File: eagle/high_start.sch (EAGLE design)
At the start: 34 parts, among them IC1 7805TV, Q1 16Mhz, Q2 IRF510, Q3 IRF510, Q4 IRF510, U2 ATMEGA328P_PDIP

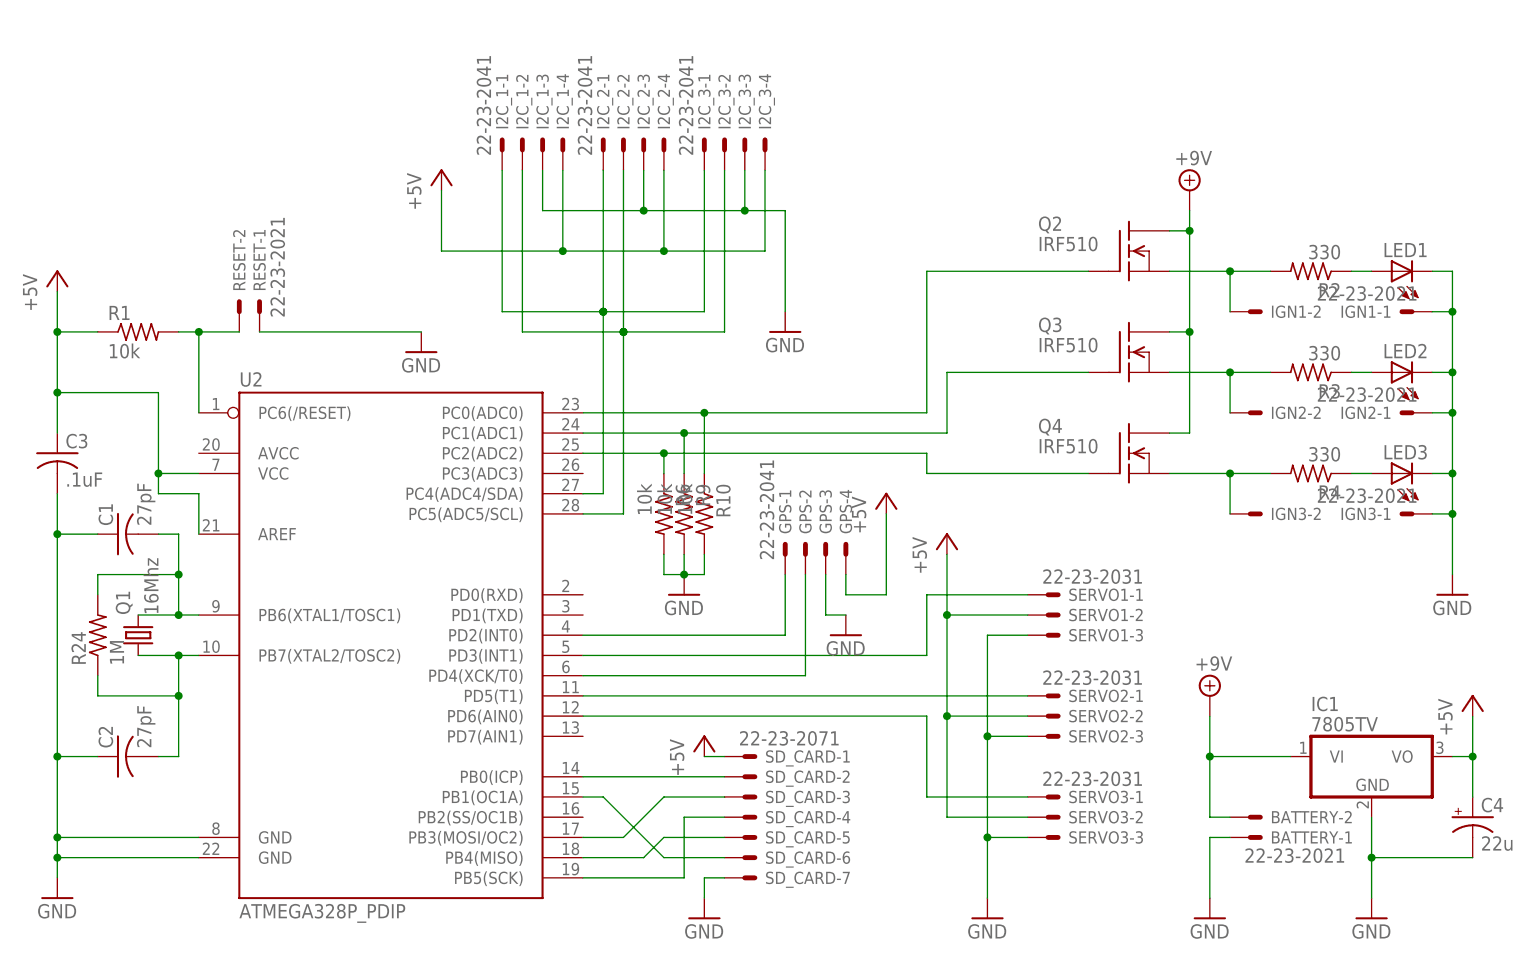
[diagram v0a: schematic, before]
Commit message: moved igniter FETs to low side
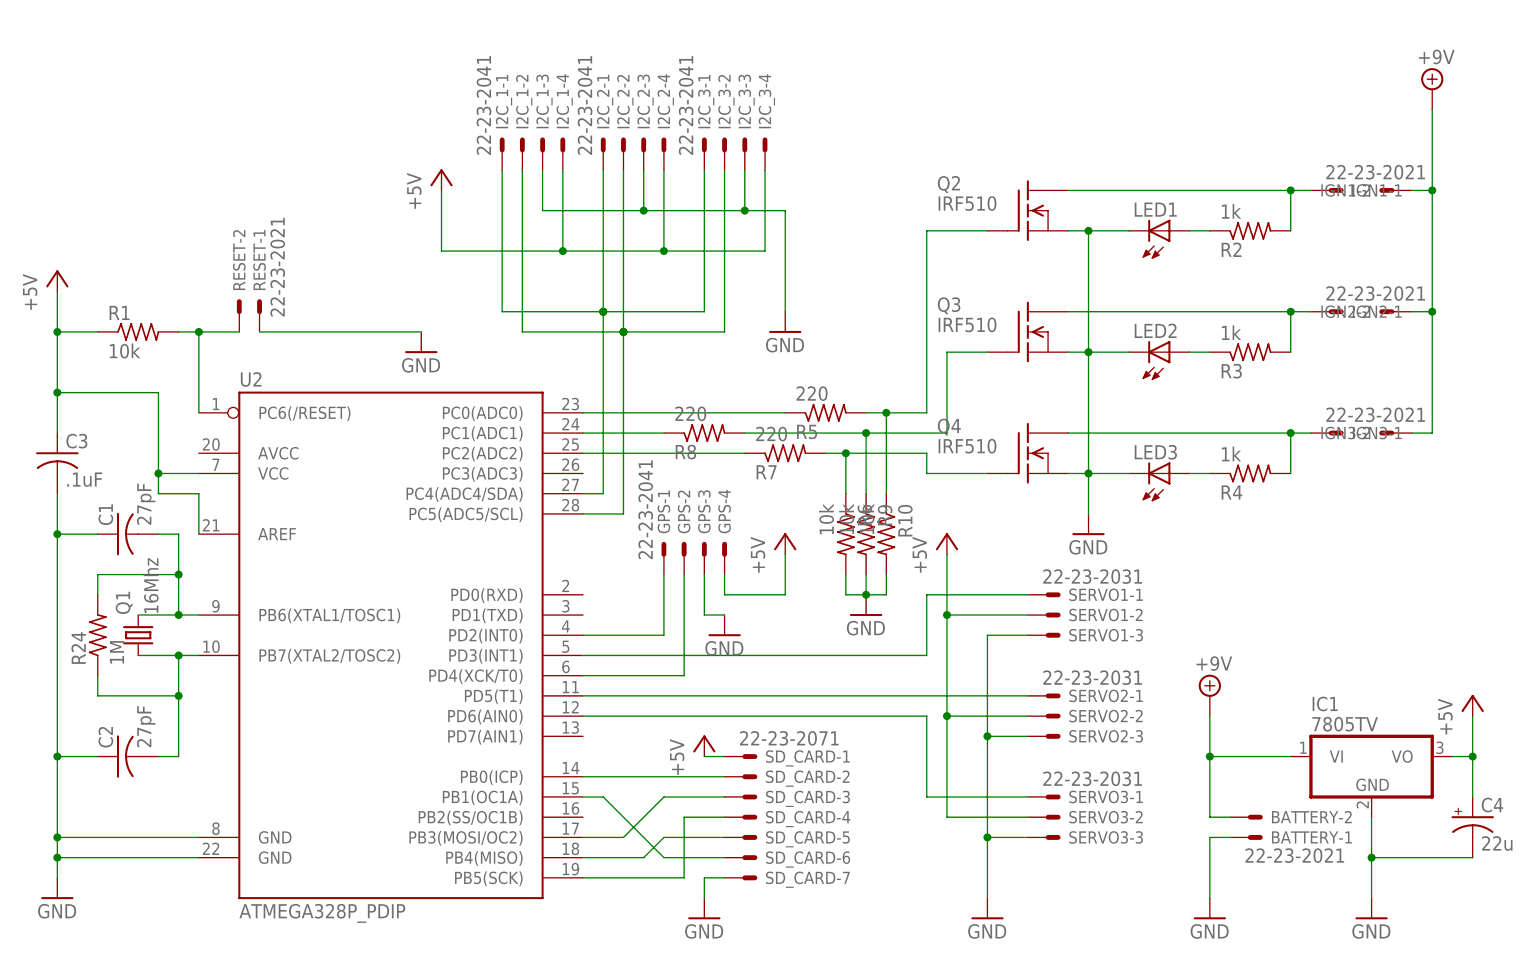
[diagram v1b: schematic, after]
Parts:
- added R5, R7, R8: 220, rcl:R-US_0207/7
- R2, R3, R4: value 330 -> 1k
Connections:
- new net N$12: IGN1-1.S, Q2.D, R2.2
- new net N$13: IGN2-1.S, Q3.D, R3.2
- new net N$14: IGN3-1.S, Q4.D, R4.2
- net +9V: now also IGN1-2.S, IGN2-2.S, IGN3-2.S; no longer Q2.D, Q3.D, Q4.D
- net GND: now also Q2.S, Q3.S, Q4.S; no longer IGN1-1.S, IGN2-1.S, IGN3-1.S
- net N$18: now also R5.2; no longer U2.PC0(ADC0)
- net N$19: now also R8.2; no longer U2.PC1(ADC1)
- net N$20: now also R7.2; no longer U2.PC2(ADC2)
- net N$24: now also R5.1, U2.PC0(ADC0); no longer IGN1-2.S, Q2.S, R2.2
- net N$25: now also R7.1, U2.PC2(ADC2); no longer IGN2-2.S, Q3.S, R3.2
- net N$26: now also R8.1, U2.PC1(ADC1); no longer IGN3-2.S, Q4.S, R4.2
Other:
- moved on the sheet: GPS-1, GPS-2, GPS-3, GPS-4, IGN1-1, IGN1-2, IGN2-1, IGN2-2, IGN3-1, IGN3-2, LED1, LED2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

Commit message: janky rerouted
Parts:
- R10, R6, R9: device rcl:R-US_0207/2V -> rcl:R-US_0207/7
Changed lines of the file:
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@@
 <grid distance="0.1" unitdist="inch" unit="inch" style="lines" multiple="1" display="no" altdistance="0.01" altunitdist="inch" altunit="inch"/>
 <layers>
-<layer number="1" name="Top" color="4" fill="1" visible="no" active="no"/>
-<layer number="16" name="Bottom" color="1" fill="1" visible="no" active="no"/>
-<layer number="17" name="Pads" color="2" fill="1" visible="no" active="no"/>
-<layer number="18" name="Vias" color="2" fill="1" visible="no" active="no"/>
-<layer number="19" name="Unrouted" color="6" fill="1" visible="no" active="no"/>
-<layer number="20" name="Dimension" color="15" fill="1" visible="no" active="no"/>
-<layer number="21" name="tPlace" color="7" fill="1" visible="no" active="no"/>
-<layer number="22" name="bPlace" color="7" fill="1" visible="no" active="no"/>
-<layer number="23" name="tOrigins" color="15" fill="1" visible="no" active="no"/>
-<layer number="24" name="bOrigins" color="15" fill="1" visible="no" active="no"/>
-<layer number="25" name="tNames" color="7" fill="1" visible="no" active="no"/>
-<layer number="26" name="bNames" color="7" fill="1" visible="no" active="no"/>
-<layer number="27" name="tValues" color="7" fill="1" visible="no" active="no"/>
-<layer number="28" name="bValues" color="7" fill="1" visible="no" active="no"/>
+<layer number="1" name="Top" color="4" fill="1" visible="yes" active="no"/>
+<layer number="16" name="Bottom" color="1" fill="1" visible="yes" active="no"/>
+<layer number="17" name="Pads" color="2" fill="1" visible="yes" active="no"/>
+<layer number="18" name="Vias" color="2" fill="1" visible="yes" active="no"/>
+<layer number="19" name="Unrouted" color="6" fill="1" visible="yes" active="no"/>
+<layer number="20" name="Dimension" color="15" fill="1" visible="yes" active="no"/>
+<layer number="21" name="tPlace" color="7" fill="1" visible="yes" active="no"/>
+<layer number="22" name="bPlace" color="7" fill="1" visible="yes" active="no"/>
+<layer number="23" name="tOrigins" color="15" fill="1" visible="yes" active="no"/>
+<layer number="24" name="bOrigins" color="15" fill="1" visible="yes" active="no"/>
+<layer number="25" name="tNames" color="7" fill="1" visible="yes" active="no"/>
+<layer number="26" name="bNames" color="7" fill="1" visible="yes" active="no"/>
+<layer number="27" name="tValues" color="7" fill="1" visible="yes" active="no"/>
+<layer number="28" name="bValues" color="7" fill="1" visible="yes" active="no"/>
 <layer number="29" name="tStop" color="7" fill="3" visible="no" active="no"/>
 <layer number="30" name="bStop" color="7" fill="6" visible="no" active="no"/>
@@
 <layer number="35" name="tGlue" color="7" fill="4" visible="no" active="no"/>
 <layer number="36" name="bGlue" color="7" fill="5" visible="no" active="no"/>
-<layer number="37" name="tTest" color="7" fill="1" visible="no" active="no"/>
-<layer number="38" name="bTest" color="7" fill="1" visible="no" active="no"/>
+<layer number="37" name="tTest" color="7" fill="1" visible="yes" active="no"/>
+<layer number="38" name="bTest" color="7" fill="1" visible="yes" active="no"/>
 <layer number="39" name="tKeepout" color="4" fill="11" visible="no" active="no"/>
 <layer number="40" name="bKeepout" color="1" fill="11" visible="no" active="no"/>
@@
 <layer number="44" name="Drills" color="7" fill="1" visible="no" active="no"/>
 <layer number="45" name="Holes" color="7" fill="1" visible="no" active="no"/>
-<layer number="46" name="Milling" color="3" fill="1" visible="no" active="no"/>
-<layer number="47" name="Measures" color="7" fill="1" visible="no" active="no"/>
-<layer number="48" name="Document" color="7" fill="1" visible="no" active="no"/>
-<layer number="49" name="Reference" color="7" fill="1" visible="no" active="no"/>
-<layer number="50" name="dxf" color="7" fill="1" visible="no" active="no"/>
-<layer number="51" name="tDocu" color="7" fill="1" visible="no" active="no"/>
-<layer number="52" name="bDocu" color="7" fill="1" visible="no" active="no"/>
-<layer number="53" name="tGND_GNDA" color="7" fill="9" visible="no" active="no"/>
-<layer number="54" name="bGND_GNDA" color="1" fill="9" visible="no" active="no"/>
-<layer number="56" name="wert" color="7" fill="1" visible="no" active="no"/>
-<layer number="57" name="tCAD" color="7" fill="1" visible="no" active="no"/>
-<layer number="59" name="tCarbon" color="7" fill="1" visible="no" active="no"/>
-<layer number="60" name="bCarbon" color="7" fill="1" visible="no" active="no"/>
+<layer number="46" name="Milling" color="3" fill="1" visible="yes" active="no"/>
+<layer number="47" name="Measures" color="7" fill="1" visible="yes" active="no"/>
+<layer number="48" name="Document" color="7" fill="1" visible="yes" active="no"/>
+<layer number="49" name="Reference" color="7" fill="1" visible="yes" active="no"/>
+<layer number="50" name="dxf" color="7" fill="1" visible="yes" active="no"/>
+<layer number="51" name="tDocu" color="7" fill="1" visible="yes" active="no"/>
+<layer number="52" name="bDocu" color="7" fill="1" visible="yes" active="no"/>
+<layer number="53" name="tGND_GNDA" color="7" fill="9" visible="yes" active="no"/>
+<layer number="54" name="bGND_GNDA" color="1" fill="9" visible="yes" active="no"/>
+<layer number="56" name="wert" color="7" fill="1" visible="yes" active="no"/>
+<layer number="57" name="tCAD" color="7" fill="1" visible="yes" active="no"/>
+<layer number="59" name="tCarbon" color="7" fill="1" visible="yes" active="no"/>
+<layer number="60" name="bCarbon" color="7" fill="1" visible="yes" active="no"/>
 <layer number="90" name="Modules" color="5" fill="1" visible="yes" active="yes"/>
 <layer number="91" name="Nets" color="2" fill="1" visible="yes" active="yes"/>
@@
 <part name="BATTERY" library="con-molex" deviceset="22-23-2021" device=""/>
 <part name="GND9" library="supply1" deviceset="GND" device=""/>
-<part name="R6" library="rcl" deviceset="R-US_" device="0207/2V" value="10k"/>
-<part name="R9" library="rcl" deviceset="R-US_" device="0207/2V" value="10k"/>
-<part name="R10" library="rcl" deviceset="R-US_" device="0207/2V" value="10k"/>
+<part name="R6" library="rcl" deviceset="R-US_" device="0207/7" value="10k"/>
+<part name="R9" library="rcl" deviceset="R-US_" device="0207/7" value="10k"/>
+<part name="R10" library="rcl" deviceset="R-US_" device="0207/7" value="10k"/>
 <part name="GND5" library="supply1" deviceset="GND" device=""/>
 <part name="R5" library="rcl" deviceset="R-US_" device="0207/7" value="220"/>

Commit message: improved reroute
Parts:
- R10, R6, R9: device rcl:R-US_0207/7 -> rcl:R-US_0207/5V
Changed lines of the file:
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@@
 <part name="BATTERY" library="con-molex" deviceset="22-23-2021" device=""/>
 <part name="GND9" library="supply1" deviceset="GND" device=""/>
-<part name="R6" library="rcl" deviceset="R-US_" device="0207/7" value="10k"/>
-<part name="R9" library="rcl" deviceset="R-US_" device="0207/7" value="10k"/>
-<part name="R10" library="rcl" deviceset="R-US_" device="0207/7" value="10k"/>
+<part name="R6" library="rcl" deviceset="R-US_" device="0207/5V" value="10k"/>
+<part name="R9" library="rcl" deviceset="R-US_" device="0207/5V" value="10k"/>
+<part name="R10" library="rcl" deviceset="R-US_" device="0207/5V" value="10k"/>
 <part name="GND5" library="supply1" deviceset="GND" device=""/>
 <part name="R5" library="rcl" deviceset="R-US_" device="0207/7" value="220"/>
